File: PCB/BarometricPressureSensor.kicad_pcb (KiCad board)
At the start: 2 copper layers, 104.1 x 67.1 mm, 43 parts, among them J1 USB4105-GF-A, J2 54-00125, J3 Conn_01x02, J4 GTFP08441BEU, J5 2337019-1, J6 B3B-XH-A, J7 B6B-XH-A, U1 ESP32-S3-DEVKITC-1-N16R8V, U2 DPS368XTSA1, U3 BQ24074RGT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

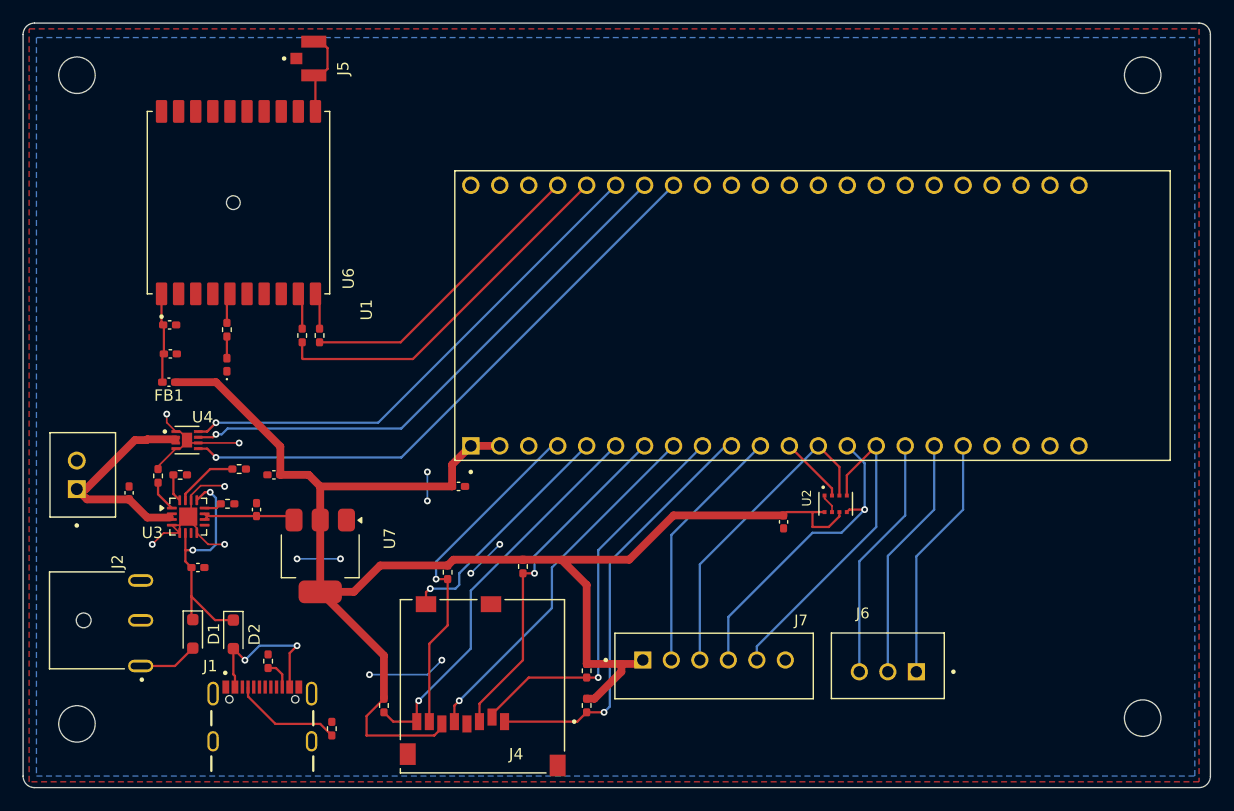
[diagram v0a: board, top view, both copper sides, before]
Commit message: Add files via upload
Updated the switch we are using for the PCB. Will need to order these switches on our own.
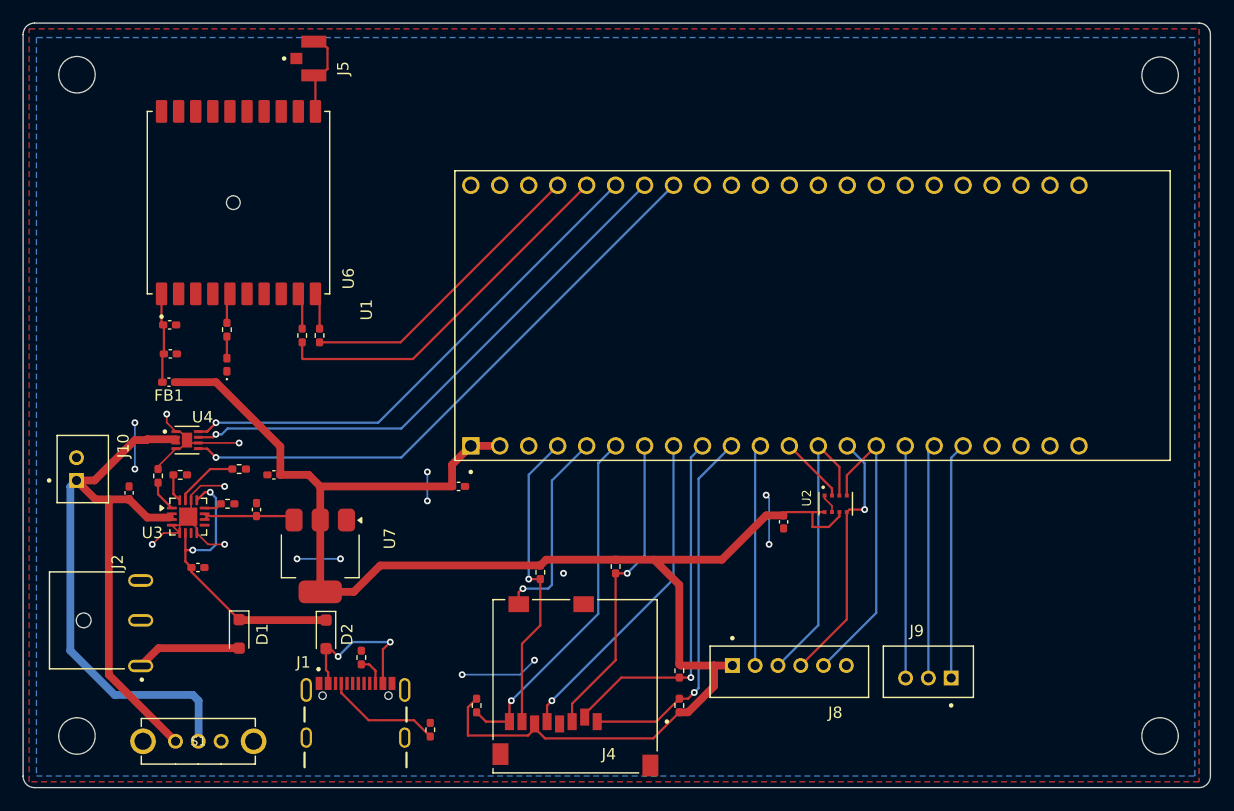
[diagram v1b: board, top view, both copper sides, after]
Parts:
- removed J3: Conn_01x02, B2B_XH_A:JST_B2B-XH-A
- removed J6: B3B-XH-A, B3B_XH_A:JST_B3B-XH-A
- removed J7: B6B-XH-A, B6B_XH_A:JST_B6B-XH-A
- added J10: B2B-PH-K-S, B2B_PH_K_S:JST_B2B-PH-K-S, F.Cu at (72.6, 143.3)
- added J8: B6B-PH-K-S, B6B_PH_K_S:JST_B6B-PH-K-S, F.Cu at (134.6, 161.0)
- added J9: B3B-PH-K-S, B3B_PH_K_S:JST_B3B-PH-K-S, F.Cu at (146.8, 161.0)
- added S1: EG1213, EG1213:SW_EG1213, F.Cu at (82.8, 167.1)
- moved R1 8.64 mm to (103.1, 166.1)
- moved J1 8.18 mm to (96.6, 166.8)
- moved R2 8.18 mm to (97.1, 159.8)
- moved D2 8.13 mm to (94.0, 157.8)
- moved J4 8.13 mm to (115.8, 168.3)
- moved R10 8.13 mm to (107.2, 164.0)
- moved R11 8.13 mm to (112.8, 152.3)
- moved R7 8.13 mm to (119.4, 151.8)
- moved R8 8.13 mm to (125.0, 164.0), turned to 90 degrees
- moved R9 8.13 mm to (125.0, 160.9)
- moved D1 4.06 mm to (86.4, 157.7)
- moved REF** 2.19 mm to (167.1, 166.7)
- moved REF** 1.53 mm to (167.1, 108.7)
- moved REF** 1.06 mm to (72.1, 166.7)
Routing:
- net +BATT: track 19.7 -> 75.2 mm
- net GND: track 46.4 -> 51.3 mm, vias 13 -> 16
- net /IN: track 21.5 -> 26.3 mm
- net /DPSMISO: track 27.5 -> 23.0 mm
- net /D2: track 37.4 -> 33.1 mm
- net Net-(D1-A): track 5.22 -> 9.28 mm
- net /SDCLK: track 32.1 -> 28.8 mm
- net /D3: track 35.0 -> 31.6 mm
- net /D1: track 34.6 -> 31.3 mm
- net /SDDET: track 21.1 -> 17.7 mm
- net /CMD: track 30.8 -> 27.4 mm
- net /D0: track 30.6 -> 27.4 mm
- net /CS2: track 22.0 -> 19.5 mm
- net +3V3: track 139.7 -> 142.1 mm
- net /DPSMOSI: track 28.2 -> 25.8 mm
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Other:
- rule pad_to_mask_clearance: 0.03 -> 0
